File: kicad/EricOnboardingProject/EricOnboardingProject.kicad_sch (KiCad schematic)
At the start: 0 parts

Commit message: Saving kicad updates from a few days ago.
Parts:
- added L1: 220 uH, symbol Device:L
- added R1: R_US, symbol Device:R_US
- added U1: MC34063AP, Package_DIP:DIP-8_W7.62mm, symbol Regulator_Switching:MC34063AP
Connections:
- new net: L1.1, R1.2
- new net: L1.2, U1.1 (SwC)
- new net: R1.1, U1.8 (DC)

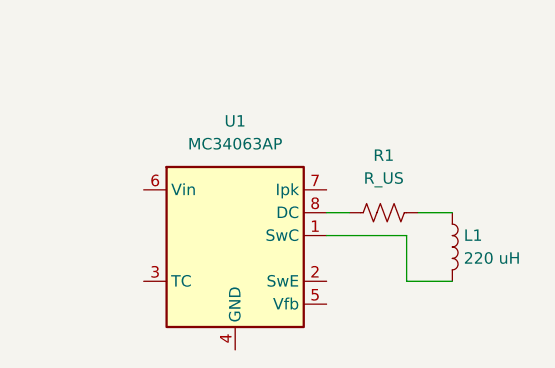
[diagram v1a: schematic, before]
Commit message: Reformated the text files and continued with KiCad schematic
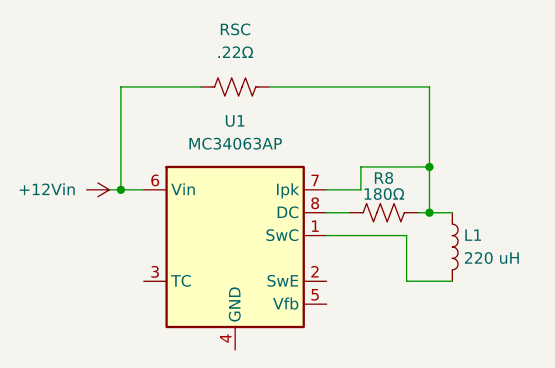
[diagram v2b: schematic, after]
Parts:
- added RSC: .22Ω, symbol Device:R_US
- R8: renamed from R1; value R_US -> 180Ω
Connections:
- net at L1.1, R8.2: now also U1.7 (Ipk), RSC.2
- net at U1.6 (Vin): now also RSC.1

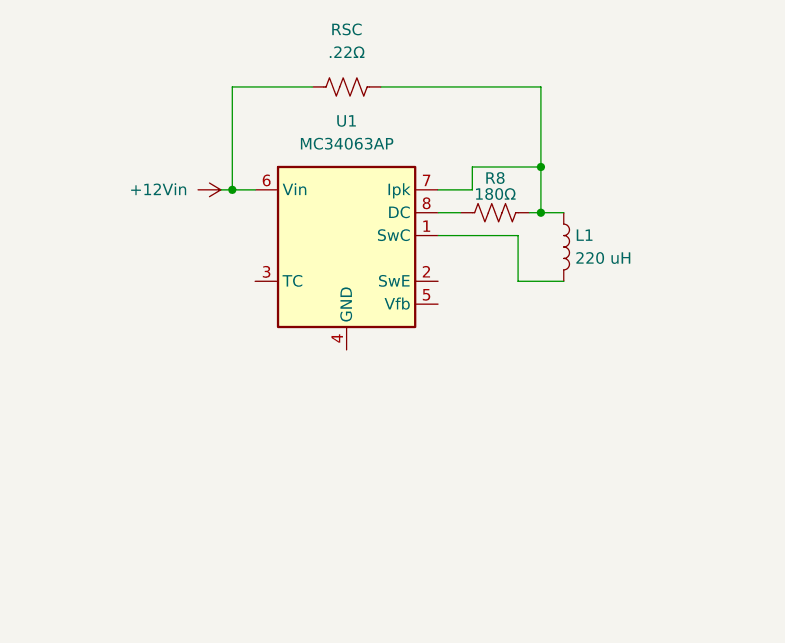
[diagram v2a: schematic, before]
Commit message: Finalized KiCad schematic, set up the PCB editor
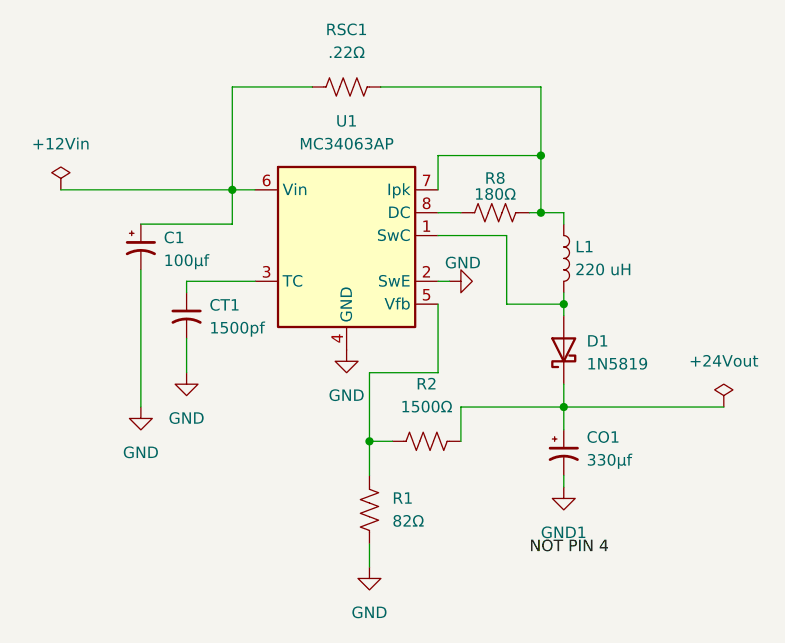
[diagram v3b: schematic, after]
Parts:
- added C1: 100μf, Capacitor_THT:CP_Radial_D6.3mm_P2.50mm, symbol Device:C_Polarized_Small_US
- added CO1: 330μf, Diode_THT:D_DO-41_SOD81_P10.16mm_Horizontal, symbol Device:C_Polarized_Small_US
- added CT1: 1500pf, Capacitor_THT:C_Disc_D5.0mm_W2.5mm_P5.00mm, symbol Device:C_Small_US
- added D1: 1N5819, Diode_THT:D_DO-41_SOD81_P10.16mm_Horizontal, symbol Diode:1N5819
- added R1: 82Ω, Resistor_THT:R_Axial_DIN0207_L6.3mm_D2.5mm_P10.16mm_Horizontal, symbol Device:R_US
- added R2: 1500Ω, Package_DIP:DIP-8_W7.62mm, symbol Device:R_US
- L1: footprint (none) -> Inductor_THT:L_Radial_D7.5mm_P5.00mm_Fastron_07P
- R8: footprint (none) -> Resistor_THT:R_Axial_DIN0207_L6.3mm_D2.5mm_P10.16mm_Horizontal
- RSC1: renamed from RSC; footprint (none) -> Resistor_THT:R_Axial_DIN0207_L6.3mm_D2.5mm_P10.16mm_Horizontal
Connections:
- net at RSC1.1, U1.6 (Vin): now also C1.1
- net at L1.2, U1.1 (SwC): now also D1.2 (A)
- net GND: now reaches U1.2 (SwE)
- net GND: now also U1.4 (GND), C1.2, CT1.2, R1.2
- net at U1.3 (TC): now also CT1.1
- net at U1.5 (Vfb): now also R1.1, R2.2
- new net: CO1.1, D1.1 (K), R2.1
- new net GND1: CO1.2
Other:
- moved on the sheet: L1

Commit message: Completed the KiCad diagram!
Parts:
- R2: footprint Package_DIP:DIP-8_W7.62mm -> Resistor_THT:R_Axial_DIN0207_L6.3mm_D2.5mm_P10.16mm_Horizontal
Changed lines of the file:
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@@
 			)
 		)
-		(property "Footprint" "Package_DIP:DIP-8_W7.62mm"
+		(property "Footprint" "Resistor_THT:R_Axial_DIN0207_L6.3mm_D2.5mm_P10.16mm_Horizontal"
 			(at 136.906 107.696 90)
 			(hide yes)

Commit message: Edited KiCad to contain actual materials
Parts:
- CT1: value 1500pf -> 680pf
- R1: value 82Ω -> 100Ω + 10Ω +10Ω
- R2: value 1500Ω -> 2200Ω
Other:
- note added: "R1 and R2 updated to fit given parts"
- note added: "^Formerly 1500pf"
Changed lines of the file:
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@@
 		(comment 4 "${MRC_SUBSYSTEM}")
+	)
+	(text "^Formerly\n1500pf"
+		(exclude_from_sim no)
+		(at 117.856 98.044 0)
+		(effects
+			(font
+				(size 1.27 1.27)
+			)
+		)
+	)
+	(text "R1 and R2 updated \nto fit given parts"
+		(exclude_from_sim no)
+		(at 102.616 119.126 0)
+		(effects
+			(font
+				(size 1.27 1.27)
+			)
+		)
 	)
 	(junction
@@
 			)
 		)
-		(property "Value" "82Ω"
+		(property "Value" "100Ω + 10Ω +10Ω"
 			(at 133.35 115.5699 0)
 			(show_name no)
@@
 			)
 		)
-		(property "Value" "1500Ω"
+		(property "Value" "2200Ω"
 			(at 137.16 102.87 90)
 			(show_name no)
@@
 			)
 		)
-		(property "Value" "1500pf"
+		(property "Value" "680pf"
 			(at 113.03 94.1069 0)
 			(show_name no)
